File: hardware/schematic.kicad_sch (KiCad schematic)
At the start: 3 parts

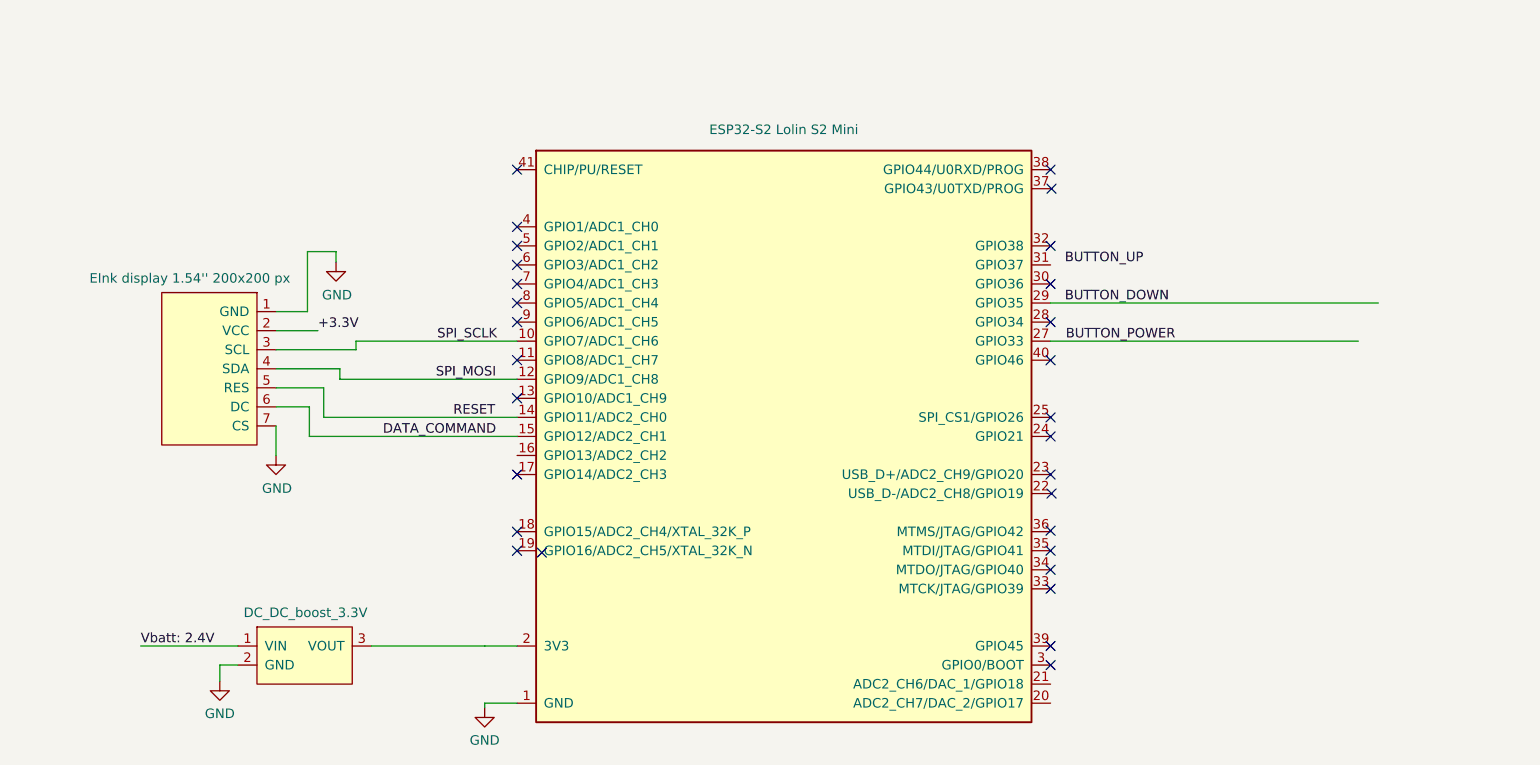
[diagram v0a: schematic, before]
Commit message: Added correct ESP32-S2 symbol
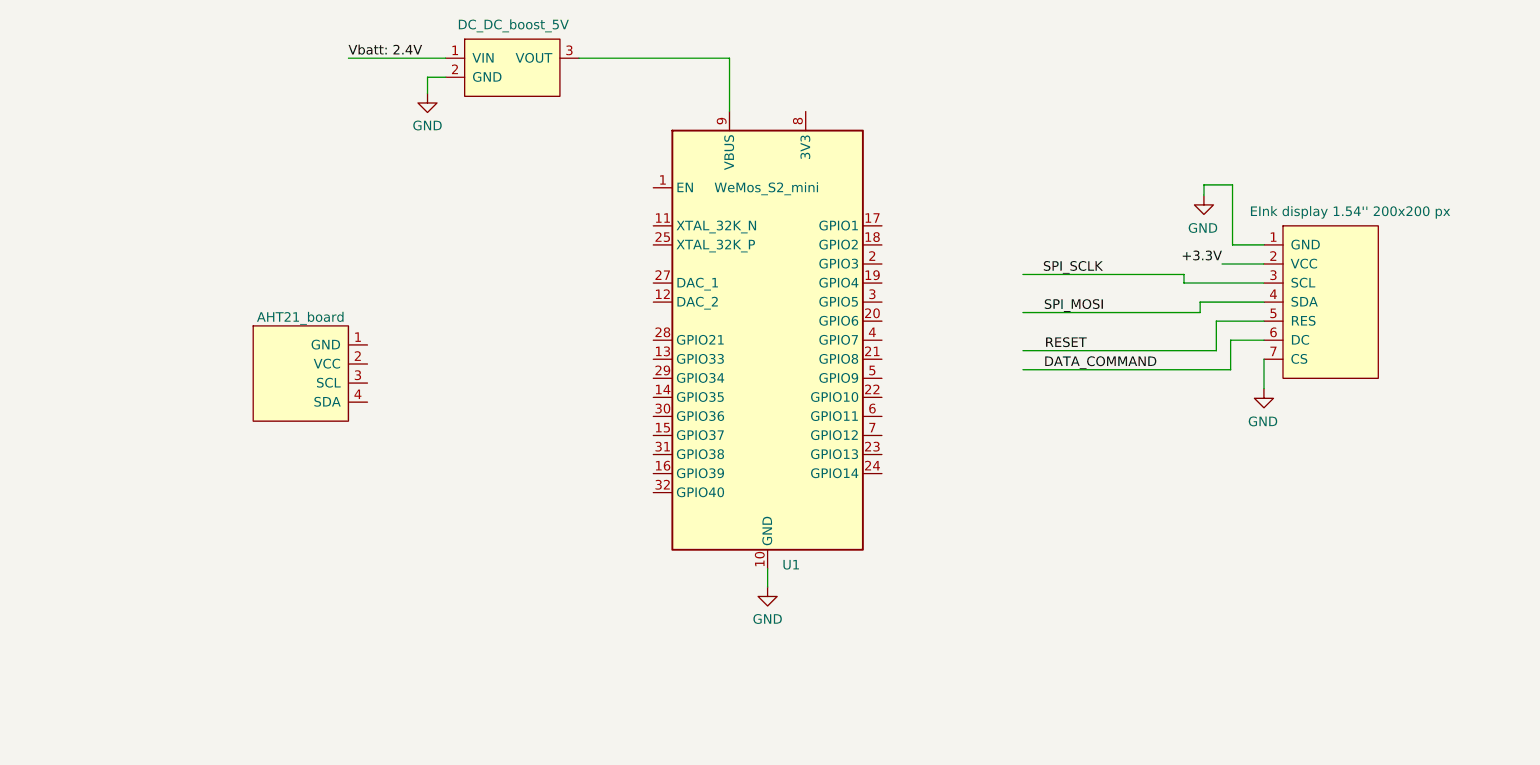
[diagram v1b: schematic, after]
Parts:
- removed NA?: DC_DC_boost_3.3V, symbol dc_dc_boost_3.3v:DC_DC_boost_3.3V
- removed U?: ESP32-S2 Lolin S2 Mini, Espressif:ESP32-S2-WROOM, symbol Espressif:ESP32-S2-WROOM
- added NA1: DC_DC_boost_5V, symbol dc_dc_boost_3.3v:DC_DC_boost_3.3V
- added NA2: AHT21_board, symbol AHT21:AHT21
- added U1: WeMos_S2_mini, Module:WEMOS_S2_mini, symbol esp32:WeMos_S2_mini
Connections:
- net GND: now also NA1.2 (GND), U1.10 (GND), U1.26 (GND)
- net Vbatt: 2.4V: now also NA1.1 (VIN)
- new net: NA1.3 (VOUT), U1.9 (VBUS)
- no-connect marks 29 -> 0
